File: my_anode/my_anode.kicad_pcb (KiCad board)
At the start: 2 copper layers, 163 x 163 mm, 41 parts, among them J3 430451019, J4 430450419

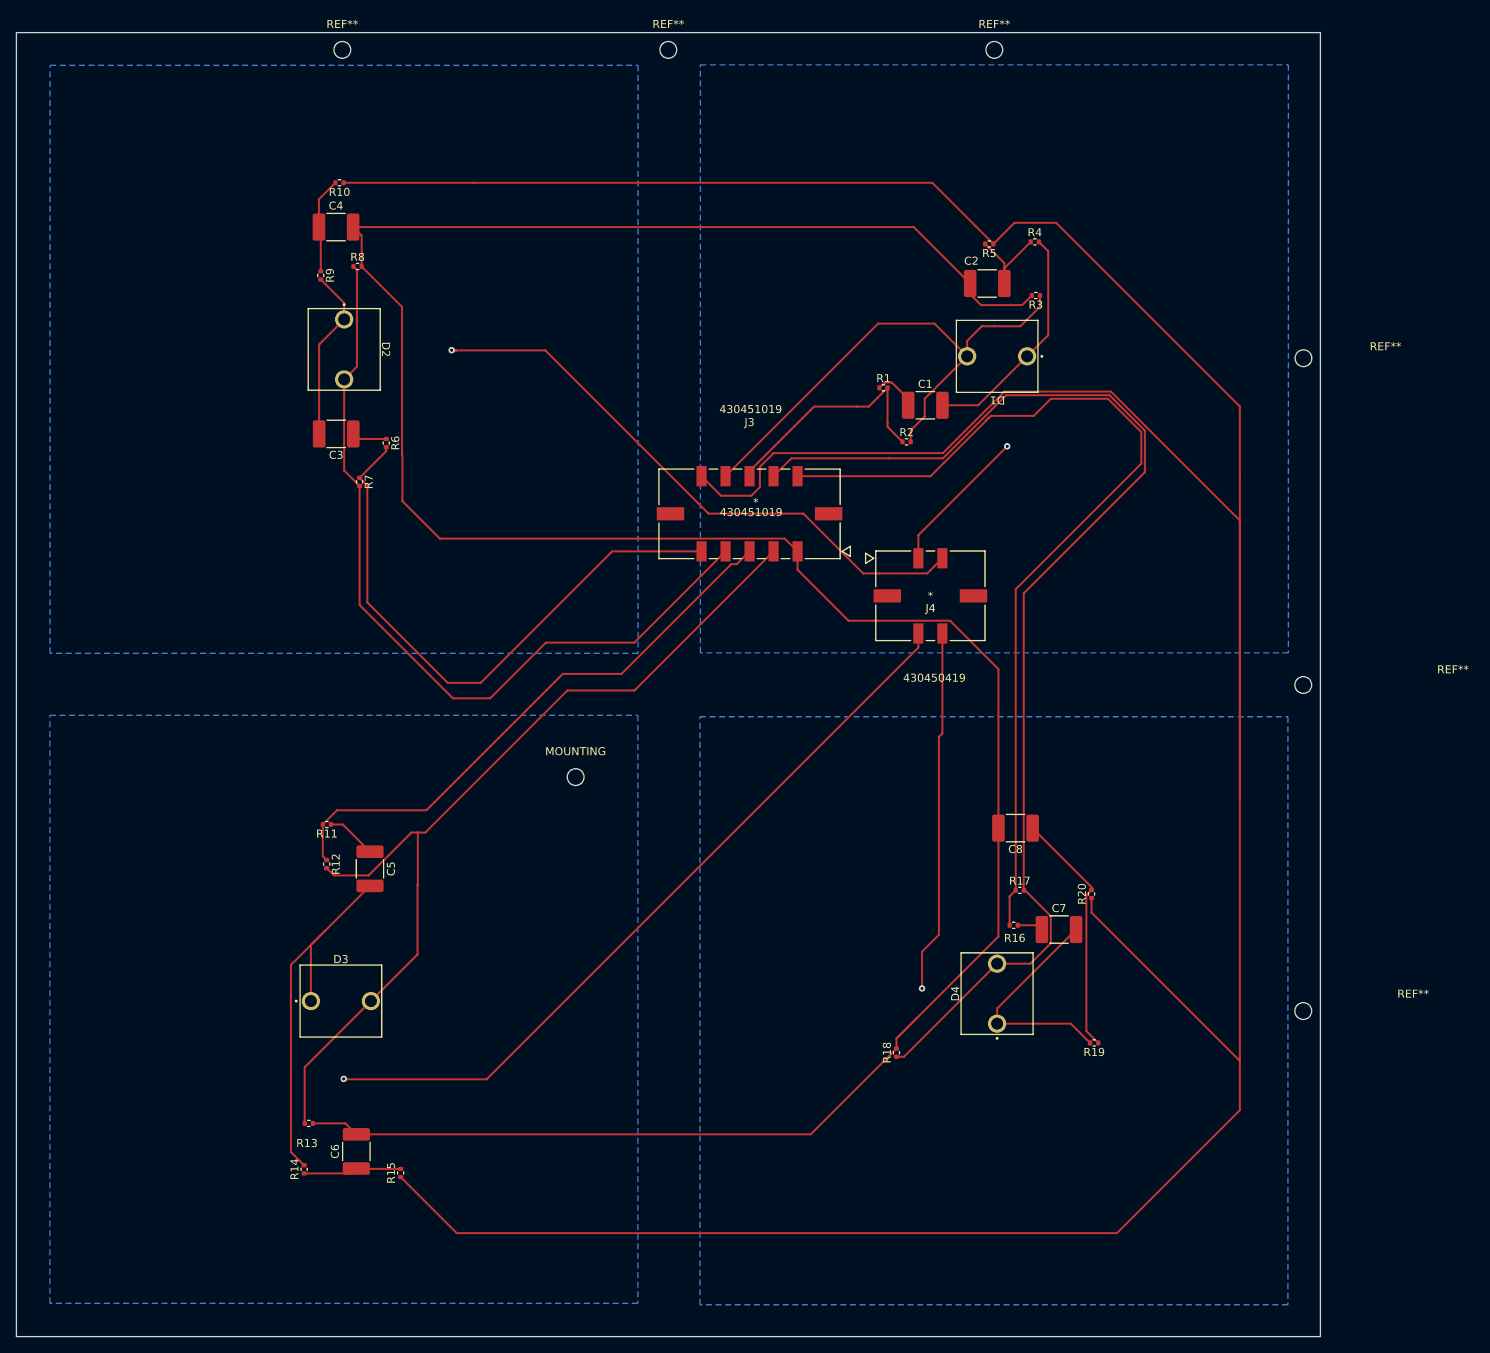
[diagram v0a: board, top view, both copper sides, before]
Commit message: V1 with voltage divider
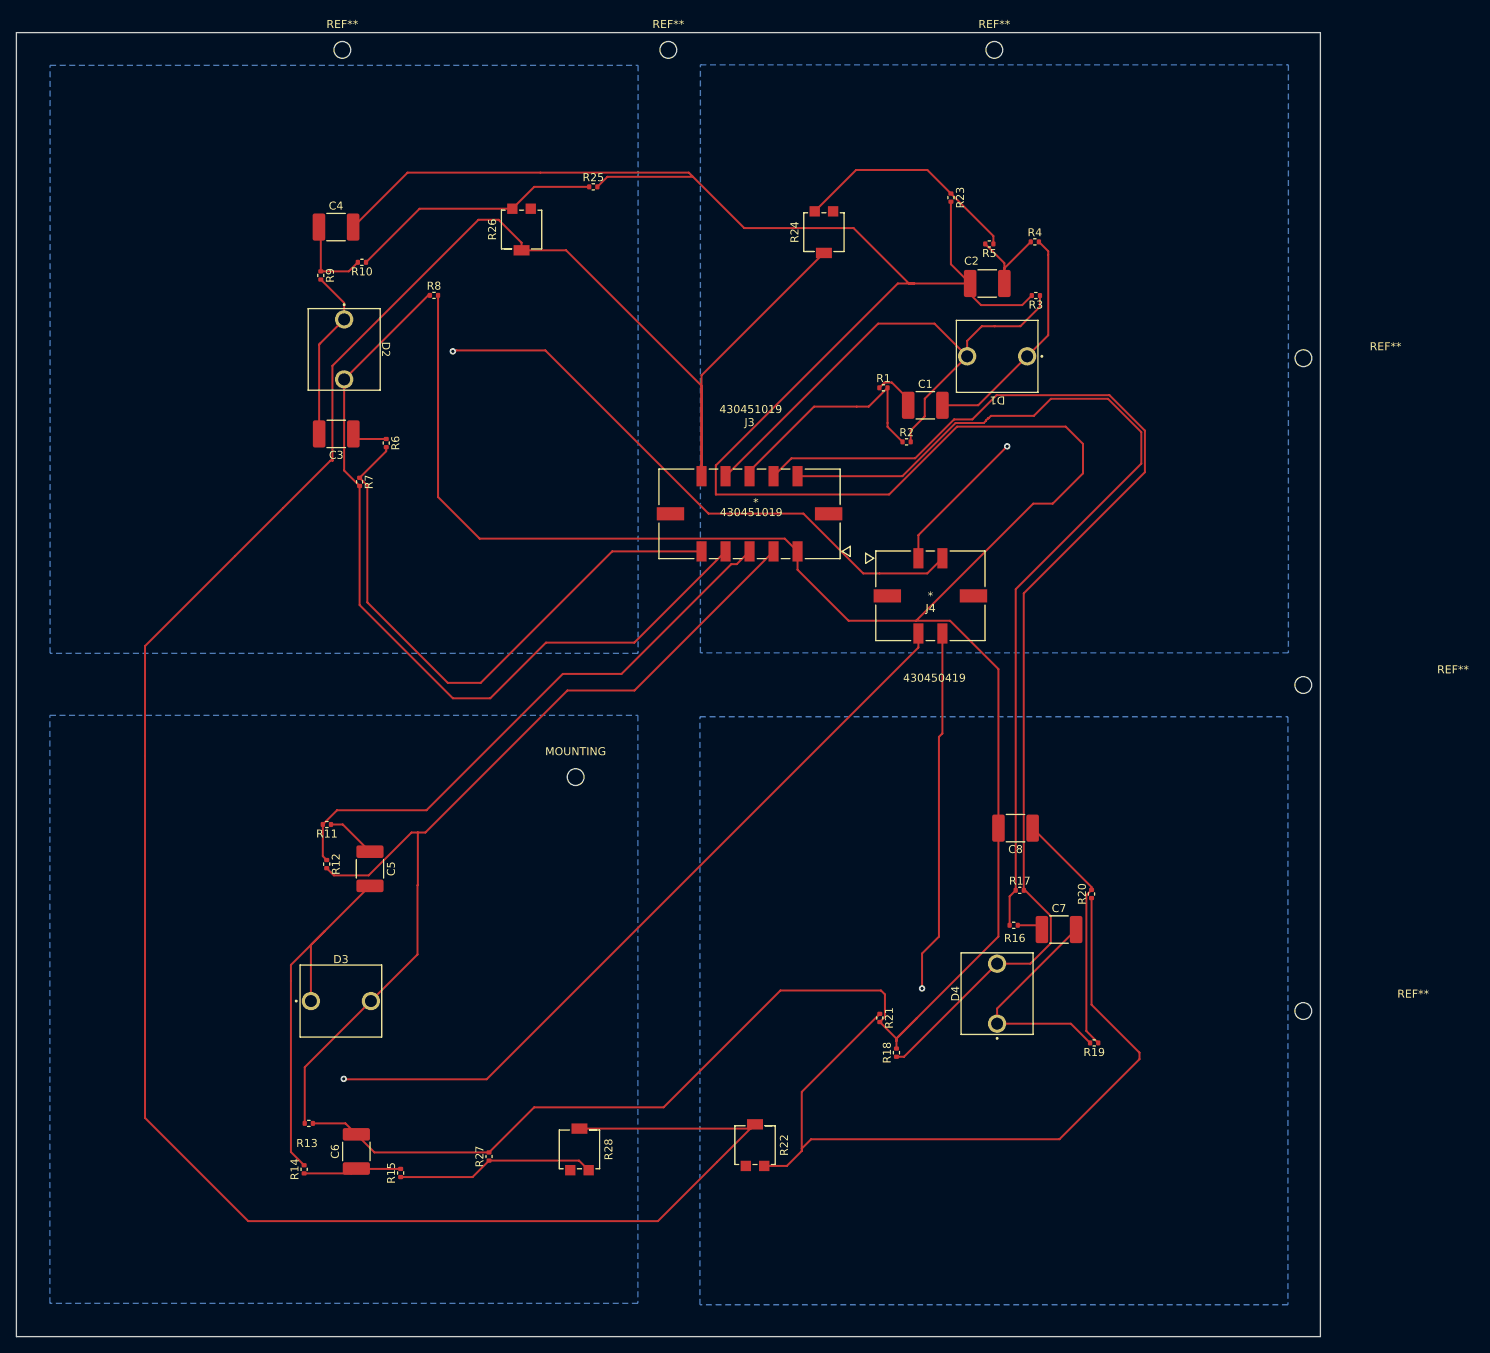
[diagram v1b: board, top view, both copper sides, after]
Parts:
- added R21: R_US, Resistor_SMD:R_0402_1005Metric, F.Cu at (228.2, 240.2)
- added R22: R_Variable_US, Potentiometer_SMD:Potentiometer_Bourns_3214G_Horizontal, F.Cu at (212.6, 256.1)
- added R23: R_US, Resistor_SMD:R_0402_1005Metric, F.Cu at (237.1, 137.7)
- added R24: R_Variable_US, Potentiometer_SMD:Potentiometer_Bourns_3214G_Horizontal, F.Cu at (221.2, 142.0)
- added R25: R_US, Resistor_SMD:R_0402_1005Metric, F.Cu at (192.4, 136.3)
- added R26: R_Variable_US, Potentiometer_SMD:Potentiometer_Bourns_3214G_Horizontal, F.Cu at (183.4, 141.7)
- added R27: R_US, Resistor_SMD:R_0402_1005Metric, F.Cu at (179.3, 257.6)
- added R28: R_Variable_US, Potentiometer_SMD:Potentiometer_Bourns_3214G_Horizontal, F.Cu at (190.7, 256.7)
- moved R10 10.3 mm to (163.5, 145.8)
- moved R8 10.2 mm to (172.5, 149.9)
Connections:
- net zone1 renamed Net-(J4-Pad1)
- net zone2 renamed Net-(J4-Pad2)
- net zone3 renamed Net-(J4-Pad3)
- net zone4 renamed Net-(J4-Pad4)
- R10 pad 1: /B1 -> Net-(R10-Pad1)
- R15 pad 1: /B1 -> Net-(R15-Pad1)
- R20 pad 1: /B1 -> Net-(R20-Pad1)
- R5 pad 1: /B1 -> Net-(R5-Pad1)
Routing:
- net /B1: track 472.4 -> 321.1 mm
- net /1G1: track 345.4 -> 489.9 mm
- net Net-(R20-Pad1): track 0.00 -> 96.1 mm
- net Net-(R10-Pad1): track 0.00 -> 31.8 mm
- net Net-(R5-Pad1): track 0.00 -> 28.9 mm
- net Net-(R15-Pad1): track 0.00 -> 24.9 mm
- net Net-(C4-Pad1): track 12.0 -> 10.7 mm
- net Net-(C5-Pad2): track 49.6 -> 49.1 mm

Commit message: Add anode prior to copying
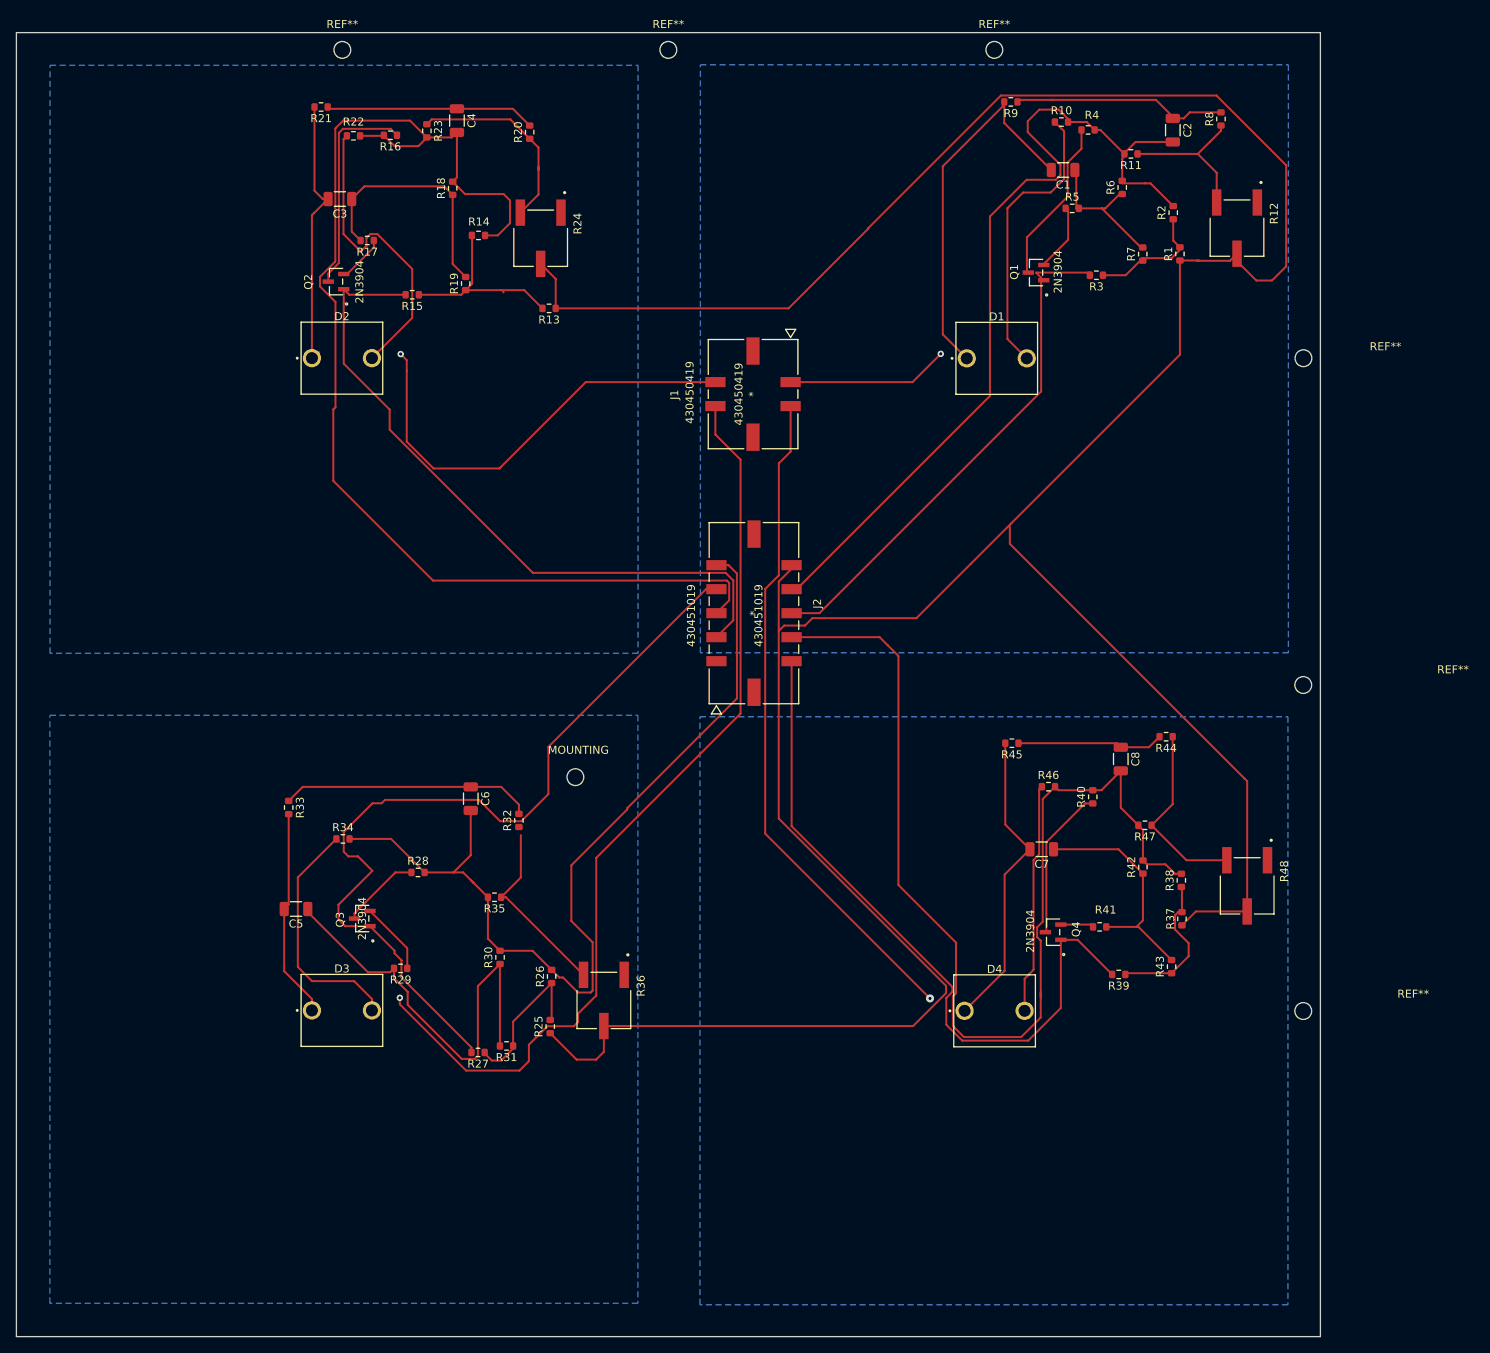
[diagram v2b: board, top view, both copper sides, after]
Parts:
- removed J3: 430451019, footprints:430451019
- removed J4: 430450419, 430450419:430450419
- added J1: 430450419, 430450419:430450419, F.Cu at (212.3, 162.3)
- added J2: 430451019, 430451019:430451019, F.Cu at (212.5, 189.6)
- added Q1: 2N3904, BC846BLT3G:BC846BLT3G, F.Cu at (247.7, 147.1)
- added Q2: 2N3904, BC846BLT3G:BC846BLT3G, F.Cu at (160.2, 148.2)
- added Q3: 2N3904, BC846BLT3G:BC846BLT3G, F.Cu at (163.5, 227.8)
- added Q4: 2N3904, BC846BLT3G:BC846BLT3G, F.Cu at (249.9, 229.5)
- added R29: R_US, Resistor_SMD:R_0603_1608Metric, F.Cu at (168.3, 234.0)
- added R30: R_US, Resistor_SMD:R_0603_1608Metric, F.Cu at (180.7, 232.7)
- added R31: R_US, Resistor_SMD:R_0603_1608Metric, F.Cu at (181.5, 243.7)
- added R32: R_US, Resistor_SMD:R_0603_1608Metric, F.Cu at (183.1, 215.5)
- added R33: R_US, Resistor_SMD:R_0603_1608Metric, F.Cu at (154.3, 213.9)
- added R34: R_US, Resistor_SMD:R_0603_1608Metric, F.Cu at (161.1, 217.9)
- added R35: R_US, Resistor_SMD:R_0603_1608Metric, F.Cu at (180.0, 225.1)
- added R36: R_Variable_US, 3361P-1-104GLF:TRIM_3361P-1-104GLF, F.Cu at (193.7, 238.0)
- added R37: R_US, Resistor_SMD:R_0603_1608Metric, F.Cu at (266.0, 227.8)
- added R38: R_US, Resistor_SMD:R_0603_1608Metric, F.Cu at (265.9, 223.0)
- added R39: R_US, Resistor_SMD:R_0603_1608Metric, F.Cu at (258.1, 234.8)
- added R40: R_US, Resistor_SMD:R_0603_1608Metric, F.Cu at (254.8, 212.6)
- added R41: R_US, Resistor_SMD:R_0603_1608Metric, F.Cu at (255.7, 228.9)
- added R42: R_US, Resistor_SMD:R_0603_1608Metric, F.Cu at (261.1, 221.4)
- added R43: R_US, Resistor_SMD:R_0603_1608Metric, F.Cu at (264.7, 233.8)
- added R44: R_US, Resistor_SMD:R_0603_1608Metric, F.Cu at (264.0, 205.1)
- added R45: R_US, Resistor_SMD:R_0603_1608Metric, F.Cu at (244.7, 205.9)
- added R46: R_US, Resistor_SMD:R_0603_1608Metric, F.Cu at (249.3, 211.3)
- added R47: R_US, Resistor_SMD:R_0603_1608Metric, F.Cu at (261.3, 216.2)
- added R48: R_Variable_US, 3361P-1-104GLF:TRIM_3361P-1-104GLF, F.Cu at (274.1, 223.7)
- C1, C2, C3, C4, C5, C6, C7, C8: footprint Capacitor_SMD:C_1812_4532Metric_Pad1.57x3.40mm_HandSolder -> Capacitor_SMD:C_1206_3216Metric
- R1, R10, R11, R13, R14, R15, R16, R17, R18, R19, R2, R20, R21, R23, R25, R27, R3, R4, R5, R6, R7, R8, R9: footprint Resistor_SMD:R_0402_1005Metric -> Resistor_SMD:R_0603_1608Metric
- R12: value R_US -> R_Variable_US; footprint Resistor_SMD:R_0402_1005Metric -> 3361P-1-104GLF:TRIM_3361P-1-104GLF
- R22, R26, R28: value R_Variable_US -> R_US; footprint Potentiometer_SMD:Potentiometer_Bourns_3214G_Horizontal -> Resistor_SMD:R_0603_1608Metric
- R24: footprint Potentiometer_SMD:Potentiometer_Bourns_3214G_Horizontal -> 3361P-1-104GLF:TRIM_3361P-1-104GLF
- moved R12 138.8 mm to (272.8, 141.5)
- moved R22 135.8 mm to (162.4, 130.0), turned to 0 degrees
- moved R21 133.6 mm to (158.4, 126.4), turned to 180 degrees
- moved R11 130.9 mm to (259.6, 132.2)
- moved R16 125.8 mm to (167.0, 129.9)
- moved R19 123.2 mm to (176.4, 148.4), turned to 90 degrees
- moved R18 121.5 mm to (174.8, 136.5)
- moved R14 118.8 mm to (178.0, 142.4), turned to 0 degrees
- moved R20 118.3 mm to (184.4, 129.5)
- moved R17 115.1 mm to (164.1, 143.1), turned to 180 degrees
- moved R15 109.8 mm to (169.7, 149.8), turned to 180 degrees
- moved R13 106.2 mm to (186.9, 151.5), turned to 180 degrees
- moved R25 105.1 mm to (187.0, 241.3), turned to 90 degrees
- moved R7 101.9 mm to (261.1, 144.8), turned to 90 degrees
- moved R8 100.8 mm to (270.8, 127.9), turned to 90 degrees
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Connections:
- C2 pad 2: /1G1 -> /G4
- C4 pad 2: /1G1 -> /G1
- C6 pad 2: /1G1 -> /G2
- C8 pad 2: /1G1 -> /G3
- D1 pad 2: /G1 -> Net-(D1-Pad2)
- D2 pad 2: /G2 -> Net-(D2-Pad2)
- D3 pad 2: /G3 -> Net-(D3-Pad2)
- D4 pad 2: /G4 -> Net-(D4-Pad2)
- R1 pad 1: Net-(C1-Pad1) -> /B1
- R1 pad 2: /S1 -> Net-(R1-Pad2)
- R10 pad 1: Net-(R10-Pad1) -> Net-(D1-Pad2)
- R10 pad 2: Net-(C4-Pad1) -> /G4
- R11 pad 1: Net-(C5-Pad1) -> Net-(R11-Pad1)
- R11 pad 2: /S3 -> /G4
- R12 pad 1: /S3 -> unconnected-(R12-Pad1)
- R12 pad 2: /G3 -> /B1
- R13 pad 1: /G3 -> /B1
- R13 pad 2: /1G1 -> Net-(R13-Pad2)
- R14 pad 1: Net-(C6-Pad1) -> Net-(R13-Pad2)
- R14 pad 2: Net-(C5-Pad2) -> /G1
- R15 pad 1: Net-(R15-Pad1) -> Net-(R13-Pad2)
- R15 pad 2: Net-(C6-Pad1) -> /S1
- R16 pad 1: Net-(C7-Pad1) -> Net-(Q2-Pad3)
- R16 pad 2: /S4 -> /G1
- R17 pad 1: /S4 -> Net-(Q2-Pad2)
- R17 pad 2: /G4 -> Net-(C3-Pad1)
- R18 pad 1: /G4 -> Net-(C3-Pad1)
- R18 pad 2: /1G1 -> /G1
- R19 pad 1: Net-(C8-Pad1) -> Net-(R13-Pad2)
- R19 pad 2: Net-(C7-Pad2) -> Net-(C3-Pad1)
- R2 pad 1: /S1 -> Net-(R1-Pad2)
- R2 pad 2: /G1 -> /G4
- R20 pad 2: Net-(C8-Pad1) -> Net-(C4-Pad1)
- R21 pad 1: Net-(R20-Pad1) -> Net-(C4-Pad1)
- R21 pad 2: /1G1 -> Net-(C3-Pad2)
- R22 pad 1: Net-(R20-Pad1) -> Net-(D2-Pad2)
- R22 pad 2: /B1 -> /G1
- R23 pad 1: Net-(R5-Pad1) -> Net-(R20-Pad1)
- R23 pad 2: /1G1 -> /G1
- R24 pad 1: Net-(R5-Pad1) -> unconnected-(R24-Pad1)
- R24 pad 3: (no net) -> Net-(R20-Pad1)
- R25 pad 1: Net-(R10-Pad1) -> /B1
- R25 pad 2: /1G1 -> Net-(R25-Pad2)
- R26 pad 1: Net-(R10-Pad1) -> Net-(R25-Pad2)
- R26 pad 2: /B1 -> /G2
- R27 pad 1: Net-(R15-Pad1) -> Net-(R25-Pad2)
- R27 pad 2: /1G1 -> /S2
- R28 pad 1: Net-(R15-Pad1) -> Net-(Q3-Pad3)
- R28 pad 2: /B1 -> /G2
- R3 pad 1: /G1 -> Net-(R1-Pad2)
- R3 pad 2: /1G1 -> /S4
- R4 pad 1: Net-(C2-Pad1) -> Net-(Q1-Pad3)
- R4 pad 2: Net-(C1-Pad2) -> /G4
- R5 pad 1: Net-(R5-Pad1) -> Net-(Q1-Pad2)
- R5 pad 2: Net-(C2-Pad1) -> Net-(C1-Pad1)
- R6 pad 1: Net-(C3-Pad1) -> Net-(C1-Pad1)
- R6 pad 2: /S2 -> /G4
- R7 pad 1: /S2 -> Net-(R1-Pad2)
- R7 pad 2: /G2 -> Net-(C1-Pad1)
- R8 pad 1: /G2 -> Net-(R11-Pad1)
- R8 pad 2: /1G1 -> Net-(C2-Pad1)
- R9 pad 1: Net-(C4-Pad1) -> Net-(C2-Pad1)
- R9 pad 2: Net-(C3-Pad2) -> Net-(C1-Pad2)
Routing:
- net /1G1: track 489.9 -> 0.00 mm
- net Net-(J1-Pad4): track 0.00 -> 116.9 mm, vias 0 -> 1
- net Net-(J4-Pad3): track 96.0 -> 0.00 mm, vias 1 -> 0
- net /B1: track 321.1 -> 407.8 mm
- net /G1: track 67.6 -> 152.2 mm
- net Net-(J1-Pad2): track 0.00 -> 84.2 mm, vias 0 -> 1
- net Net-(J4-Pad2): track 73.6 -> 0.00 mm, vias 1 -> 0
- net Net-(R20-Pad1): track 96.1 -> 25.1 mm
- net /S1: track 29.7 -> 87.0 mm
- net Net-(J1-Pad3): track 0.00 -> 55.7 mm, vias 0 -> 1
- net /S4: track 117.2 -> 65.0 mm
- net Net-(C5-Pad1): track 6.29 -> 54.4 mm
- net Net-(J4-Pad4): track 45.5 -> 0.00 mm, vias 1 -> 0
- net /G4: track 149.5 -> 110.0 mm
- net Net-(D2-Pad2): track 0.00 -> 38.5 mm
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- added copper zone on B.Cu, net (none)
- removed copper zone on B.Cu, net Net-(J4-Pad1)
- removed copper zone on B.Cu, net Net-(J4-Pad2)
- removed copper zone on B.Cu, net Net-(J4-Pad3)
- removed copper zone on B.Cu, net Net-(J4-Pad4)
